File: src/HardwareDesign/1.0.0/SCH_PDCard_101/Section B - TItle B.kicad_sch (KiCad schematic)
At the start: 41 parts, among them IC2 MCP22350T-2I/Q8X, IC3 INA219BIDCNT, T3 DMP3013SFV, T4 DMP3013SFV, T5 DMP3013SFV

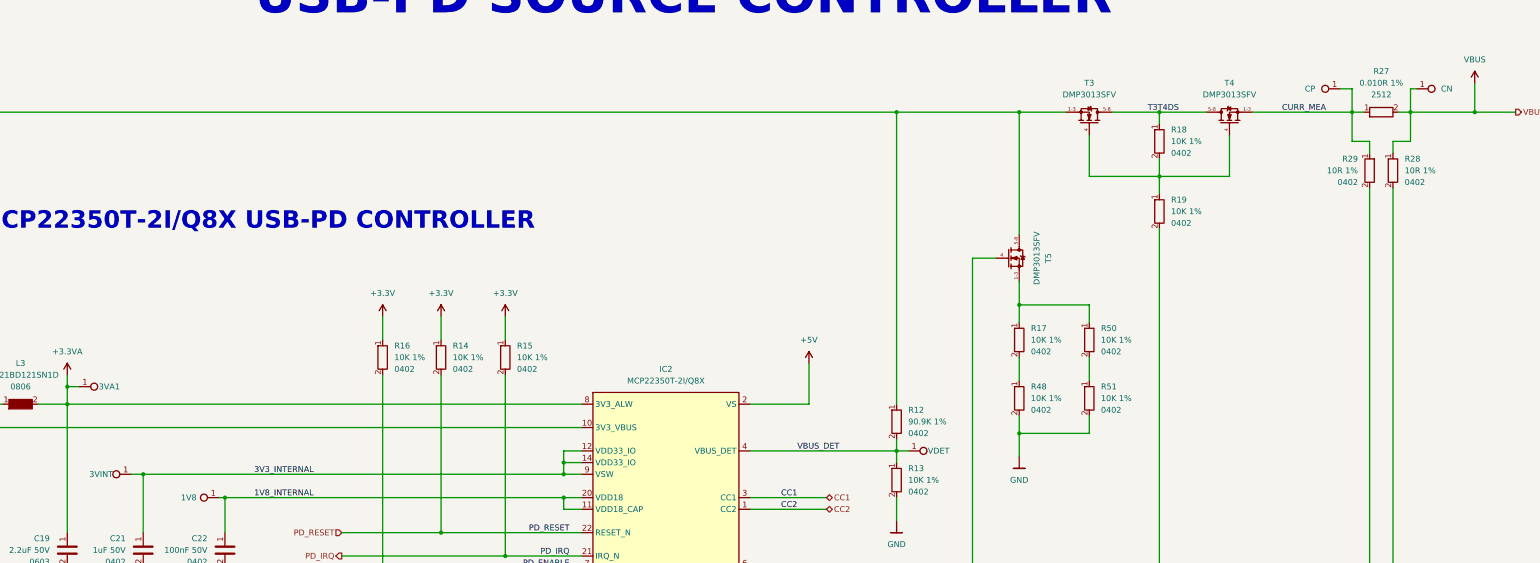
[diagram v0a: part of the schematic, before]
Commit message: update component lib
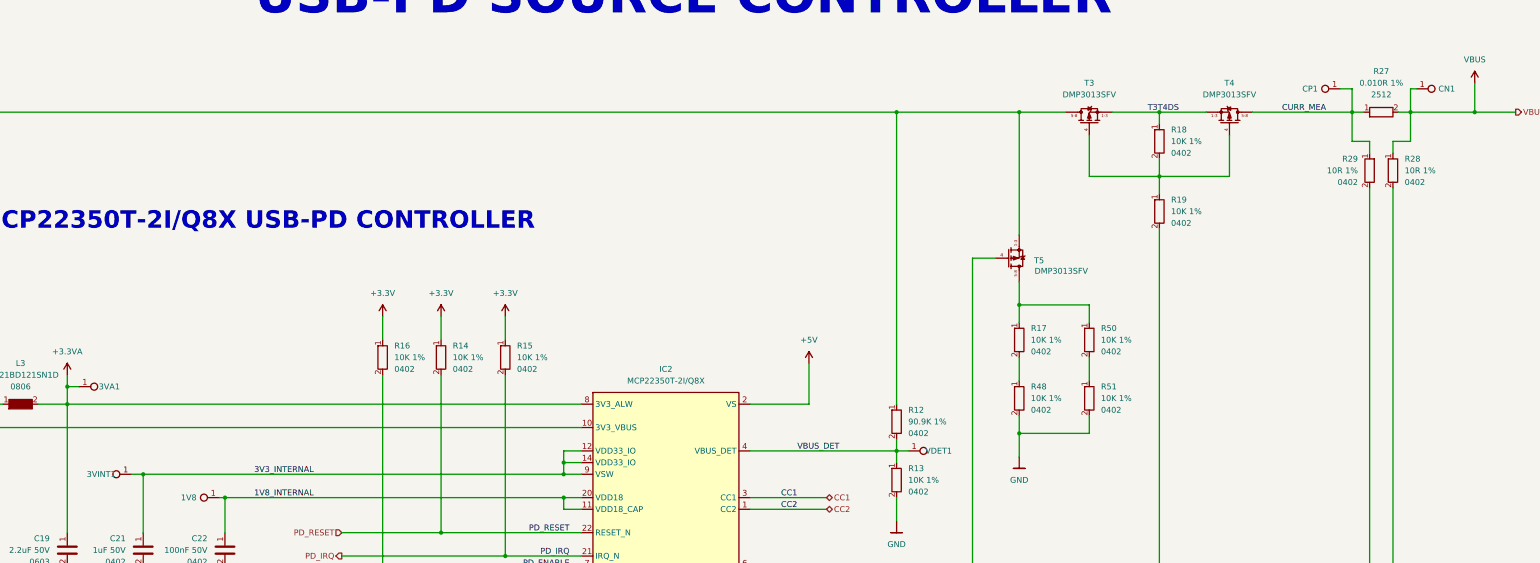
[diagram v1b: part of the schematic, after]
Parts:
- renumbered 3VINT to 3VINT1, CN to CN1, CP to CP1, VDET to VDET1
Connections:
- net CURR_MEA: now also T4.5 (D), T4.6 (D), T4.7 (D), T4.8 (D); no longer T4.1-3
- net T3T4DS: now also T3.1 (S), T3.2 (S), T3.3 (S), T4.1 (S), T4.2 (S), T4.3 (S); no longer T3.5-8, T4.5-8
- net V_SOURCE: now also T3.5 (D), T3.6 (D), T3.7 (D), T3.8 (D), T5.1 (S), T5.2 (S), T5.3 (S); no longer T3.1-3, T5.5-8
- net at R17.1, R50.1: now also T5.5 (D), T5.6 (D), T5.7 (D), T5.8 (D); no longer T5.1-3
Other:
- moved on the sheet: T3, T4
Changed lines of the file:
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@@
 		(on_board yes)
 		(dnp no)
-		(property "Reference" "CP"
+		(property "Reference" "CP1"
 			(at 346.456 46.99 90)
 			(effects
@@
 			(project "PDNode-600"
 				(path "/f9e05184-c88b-4a88-ae9c-ab2bdb32be7c/c5103ceb-5325-4a84-a025-9638a412984e/e744f3ce-03a6-44a6-8792-1447ef232b9a"
-					(reference "CP")
+					(reference "CP1")
 					(unit 1)
 				)
@@
 		(on_board yes)
 		(dnp no)
-		(property "Reference" "CN"
+		(property "Reference" "CN1"
 			(at 376.174 46.99 90)
 			(effects
@@
 			(project "PDNode-600"
 				(path "/f9e05184-c88b-4a88-ae9c-ab2bdb32be7c/c5103ceb-5325-4a84-a025-9638a412984e/e744f3ce-03a6-44a6-8792-1447ef232b9a"
-					(reference "CN")
+					(reference "CN1")
 					(unit 1)
 				)
@@
 		(on_board yes)
 		(dnp no)
-		(property "Reference" "3VINT"
+		(property "Reference" "3VINT1"
 			(at 83.566 130.81 90)
 			(effects
@@
 			(project "PDNode-600"
 				(path "/f9e05184-c88b-4a88-ae9c-ab2bdb32be7c/c5103ceb-5325-4a84-a025-9638a412984e/e744f3ce-03a6-44a6-8792-1447ef232b9a"
-					(reference "3VINT")
+					(reference "3VINT1")
 					(unit 1)
 				)
@@
 		(on_board yes)
 		(dnp no)
-		(property "Reference" "VDET"
+		(property "Reference" "VDET1"
 			(at 265.684 125.73 90)
 			(effects
@@
 			(project "PDNode-600"
 				(path "/f9e05184-c88b-4a88-ae9c-ab2bdb32be7c/c5103ceb-5325-4a84-a025-9638a412984e/e744f3ce-03a6-44a6-8792-1447ef232b9a"
-					(reference "VDET")
+					(reference "VDET1")
 					(unit 1)
 				)
@@
 		(lib_id "DS_FET:DMP3013SFV")
 		(at 283.21 83.82 0)
+		(mirror x)
 		(unit 1)
 		(exclude_from_sim no)
@@
 		(dnp no)
 		(property "Reference" "T5"
-			(at 289.56 83.82 90)
+			(at 287.528 84.328 0)
 			(effects
 				(font
@@
 		)
 		(property "Value" "DMP3013SFV"
-			(at 287.02 83.82 90)
+			(at 292.354 86.614 0)
 			(effects
 				(font
@@
 		)
 		(property "Footprint" "DS_FET:Diodes_PowerDI3333-8"
-			(at 284.988 99.06 0)
+			(at 284.988 68.58 0)
 			(show_name yes)
 			(effects
@@
 		)
 		(property "Datasheet" "https://www.diodes.com/assets/Datasheets/DMP3013SFV.pdf"
-			(at 284.988 96.774 0)
+			(at 284.988 70.866 0)
 			(show_name yes)
 			(effects
@@
 		)
 		(property "Description" "P-Channel 30 V 12A (Ta), 35A (Tc) 940mW (Ta) Surface Mount PowerDI3333-8 (Type UX)"
-			(at 284.988 92.71 0)
+			(at 284.988 74.93 0)
 			(show_name yes)
 			(effects
@@
 		)
 		(property "ROHS" "YES"
-			(at 284.988 94.742 0)
+			(at 284.988 72.898 0)
 			(show_name yes)
 			(effects
@@
 		)
 		(property "LCSC_PART" "C264098"
-			(at 284.988 90.678 0)
+			(at 284.988 76.962 0)
 			(show_name yes)
 			(effects
@@
 		)
 		(property "MPN" "DMP3013SFV"
-			(at 284.988 101.346 0)
+			(at 284.988 66.294 0)
 			(show_name yes)
 			(effects
@@
 		)
 		(property "MFR" "Infineon Technologies"
-			(at 284.988 103.632 0)
+			(at 284.988 64.008 0)
 			(show_name yes)
 			(effects
@@
 		)
 		(property "DIST1" "https://www.digikey.at/en/products/detail/diodes-incorporated/DMP3013SFV-13/8286369"
-			(at 284.988 105.664 0)
+			(at 284.988 61.976 0)
 			(show_name yes)
 			(effects
@@
 			)
 		)
-		(pin "5-8"
+		(pin "7"
 		)
-		(pin "1-3"
+		(pin "8"
 		)
 		(pin "4"
 		)
+		(pin "6"
+		)
+		(pin "5"
+		)
+		(pin "1"
+		)
+		(pin "3"
+		)
+		(pin "2"
+		)
 		(instances
 			(project "PDNode-600"
@@
 	(symbol
 		(lib_id "DS_FET:DMP3013SFV")
-		(at 298.45 52.07 270)
-		(mirror x)
+		(at 298.45 52.07 90)
 		(unit 1)
 		(exclude_from_sim no)
@@
 		(on_board yes)
 		(dnp no)
-		(fields_autoplaced yes)
 		(property "Reference" "T3"
 			(at 298.45 45.72 90)
@@
 		)
 		(property "Footprint" "DS_FET:Diodes_PowerDI3333-8"
-			(at 283.21 50.292 0)
+			(at 313.69 50.292 0)
 			(show_name yes)
 			(effects
@@
 		)
 		(property "Datasheet" "https://www.diodes.com/assets/Datasheets/DMP3013SFV.pdf"
-			(at 285.496 50.292 0)
+			(at 311.404 50.292 0)
 			(show_name yes)
 			(effects
@@
 		)
 		(property "Description" "P-Channel 30 V 12A (Ta), 35A (Tc) 940mW (Ta) Surface Mount PowerDI3333-8 (Type UX)"
-			(at 289.56 50.292 0)
+			(at 307.34 50.292 0)
 			(show_name yes)
 			(effects
@@
 		)
 		(property "ROHS" "YES"
-			(at 287.528 50.292 0)
+			(at 309.372 50.292 0)
 			(show_name yes)
 			(effects
@@
 		)
 		(property "LCSC_PART" "C264098"
-			(at 291.592 50.292 0)
+			(at 305.308 50.292 0)
 			(show_name yes)
 			(effects
@@
 		)
 		(property "MPN" "DMP3013SFV"
-			(at 280.924 50.292 0)
+			(at 315.976 50.292 0)
 			(show_name yes)
 			(effects
@@
 		)
 		(property "MFR" "Infineon Technologies"
-			(at 278.638 50.292 0)
+			(at 318.262 50.292 0)
 			(show_name yes)
 			(effects
@@
 		)
 		(property "DIST1" "https://www.digikey.at/en/products/detail/diodes-incorporated/DMP3013SFV-13/8286369"
-			(at 276.606 50.292 0)
+			(at 320.294 50.292 0)
 			(show_name yes)
 			(effects
@@
 			)
 		)
-		(pin "5-8"
+		(pin "8"
 		)
 		(pin "4"
 		)
-		(pin "1-3"
+		(pin "6"
+		)
+		(pin "7"
+		)
+		(pin "3"
+		)
+		(pin "1"
+		)
+		(pin "2"
+		)
+		(pin "5"
 		)
 		(instances
-			(project ""
+			(project "PDNode-600"
 				(path "/f9e05184-c88b-4a88-ae9c-ab2bdb32be7c/c5103ceb-5325-4a84-a025-9638a412984e/e744f3ce-03a6-44a6-8792-1447ef232b9a"
 					(reference "T3")
@@
 	(symbol
 		(lib_id "DS_FET:DMP3013SFV")
-		(at 328.93 52.07 90)
+		(at 328.93 52.07 270)
+		(mirror x)
 		(unit 1)
 		(exclude_from_sim no)
@@
 		)
 		(property "Footprint" "DS_FET:Diodes_PowerDI3333-8"
-			(at 344.17 50.292 0)
+			(at 313.69 50.292 0)
 			(show_name yes)
 			(effects
@@
 		)
 		(property "Datasheet" "https://www.diodes.com/assets/Datasheets/DMP3013SFV.pdf"
-			(at 341.884 50.292 0)
+			(at 315.976 50.292 0)
 			(show_name yes)
 			(effects
@@
 		)
 		(property "Description" "P-Channel 30 V 12A (Ta), 35A (Tc) 940mW (Ta) Surface Mount PowerDI3333-8 (Type UX)"
-			(at 337.82 50.292 0)
+			(at 320.04 50.292 0)
 			(show_name yes)
 			(effects
@@
 		)
 		(property "ROHS" "YES"
-			(at 339.852 50.292 0)
+			(at 318.008 50.292 0)
 			(show_name yes)
 			(effects
@@
 		)
 		(property "LCSC_PART" "C264098"
-			(at 335.788 50.292 0)
+			(at 322.072 50.292 0)
 			(show_name yes)
 			(effects
@@
 		)
 		(property "MPN" "DMP3013SFV"
-			(at 346.456 50.292 0)
+			(at 311.404 50.292 0)
 			(show_name yes)
 			(effects
@@
 		)
 		(property "MFR" "Infineon Technologies"
-			(at 348.742 50.292 0)
+			(at 309.118 50.292 0)
 			(show_name yes)
 			(effects
@@
 		)
 		(property "DIST1" "https://www.digikey.at/en/products/detail/diodes-incorporated/DMP3013SFV-13/8286369"
-			(at 350.774 50.292 0)
+			(at 307.086 50.292 0)
 			(show_name yes)
 			(effects
@@
 			)
 		)
-		(pin "5-8"
+		(pin "7"
 		)
-		(pin "1-3"
+		(pin "2"
 		)
 		(pin "4"
 		)
+		(pin "1"
+		)
+		(pin "8"
+		)
+		(pin "3"
+		)
+		(pin "6"
+		)
+		(pin "5"
+		)
 		(instances
